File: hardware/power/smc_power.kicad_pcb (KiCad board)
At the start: 2 copper layers, 0 parts

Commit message: hw(power): label SW/BOOT/FB nets, add SW_NODE/BOOT_NODE classes, ERC clean, closes #34
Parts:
- added C1: 100nF, 25V, Capacitor_SMD:C_0805_2012Metric_Pad1.18x1.45mm_HandSolder, F.Cu at (43.1, 57.6)
- added C10: 24pF, 25V, Capacitor_SMD:C_0805_2012Metric_Pad1.18x1.45mm_HandSolder, F.Cu at (43.1, 66.6)
- added C11: 5.1nF, 25V, Capacitor_SMD:C_0805_2012Metric_Pad1.18x1.45mm_HandSolder, F.Cu at (43.1, 69.6)
- added C12: 100nF, 25V, Capacitor_SMD:C_0805_2012Metric_Pad1.18x1.45mm_HandSolder, F.Cu at (43.1, 72.7)
- added C13: 2.2uF, 100V, Capacitor_SMD:C_1206_3216Metric_Pad1.33x1.80mm_HandSolder, F.Cu at (53.3, 86.2)
- added C14: 2.2uF, 100V, Capacitor_SMD:C_1206_3216Metric_Pad1.33x1.80mm_HandSolder, F.Cu at (53.3, 89.5)
- added C15: 2.2uF, 100V, Capacitor_SMD:C_1206_3216Metric_Pad1.33x1.80mm_HandSolder, F.Cu at (53.3, 92.9)
- added C16: 47uF, 25V, Capacitor_THT:CP_Radial_D5.0mm_P2.50mm, F.Cu at (76.0, 79.5)
- added C17: 43pF, 25V, Capacitor_SMD:C_0805_2012Metric_Pad1.18x1.45mm_HandSolder, F.Cu at (47.9, 57.6)
- added C18: 2.2nF, 25V, Capacitor_SMD:C_0805_2012Metric_Pad1.18x1.45mm_HandSolder, F.Cu at (47.9, 60.6)
- added C19: 100nF 100V, Capacitor_SMD:C_0805_2012Metric_Pad1.18x1.45mm_HandSolder, F.Cu at (47.9, 63.6)
- added C2: 2.2uF, 100V, Capacitor_SMD:C_1206_3216Metric_Pad1.33x1.80mm_HandSolder, F.Cu at (53.3, 69.4)
- added C20: 470uF 100V, Capacitor_THT:CP_Radial_D16.0mm_P7.50mm, F.Cu at (28.2, 44.5)
- added C21: 470uF 100V, Capacitor_THT:CP_Radial_D16.0mm_P7.50mm, F.Cu at (28.2, 62.0)
- added C22: 0.33uF, Package_TO_SOT_SMD:SOT-89-3, F.Cu at (44.1, 77.3)
- added C23: 0.1uF, Package_TO_SOT_SMD:SOT-89-3, F.Cu at (44.1, 83.4)
- added C24: 4.7uF, Package_TO_SOT_SMD:SOT-89-3, F.Cu at (44.1, 89.5)
- added C25: 100nF 25V, Capacitor_SMD:C_0805_2012Metric_Pad1.18x1.45mm_HandSolder, F.Cu at (47.9, 66.6)
- added C26: 1uF 25V, Capacitor_SMD:C_0805_2012Metric_Pad1.18x1.45mm_HandSolder, F.Cu at (47.9, 69.6)
- added C3: 2.2uF, 100V, Capacitor_SMD:C_1206_3216Metric_Pad1.33x1.80mm_HandSolder, F.Cu at (53.3, 72.8)
- added C4: 2.2uF, 100V, Capacitor_SMD:C_1206_3216Metric_Pad1.33x1.80mm_HandSolder, F.Cu at (53.3, 76.1)
- added C5: 1uF, Capacitor_SMD:C_0805_2012Metric_Pad1.18x1.45mm_HandSolder, F.Cu at (43.1, 60.6)
- added C6: 1uF, Capacitor_SMD:C_0805_2012Metric_Pad1.18x1.45mm_HandSolder, F.Cu at (43.1, 63.6)
- added C7: 68uF, 50V, Capacitor_THT:CP_Radial_D8.0mm_P3.50mm, F.Cu at (70.6, 40.5)
- added C8: 10uF, 50V, Capacitor_SMD:C_1206_3216Metric_Pad1.33x1.80mm_HandSolder, F.Cu at (53.3, 79.5)
- added C9: 10uF, 50V, Capacitor_SMD:C_1206_3216Metric_Pad1.33x1.80mm_HandSolder, F.Cu at (53.3, 82.8)
- added D1: 100V 3A <= 850mV, Diode_SMD:D_SMB-SMC_Universal_Handsoldering, F.Cu at (61.2, 39.6)
- added D2: 100V 5A, Package_TO_SOT_SMD:TO-252-2, F.Cu at (71.8, 60.3)
- added D3: MBR10100, Step Motor Controller:TO508P482X997X1956-2P, F.Cu at (73.5, 53.4)
- added D4: SMBJ58A, Diode_SMD:D_SMA-SMB_Universal_Handsoldering, F.Cu at (60.6, 46.2)
- added D5: SS510, PCM_JLCPCB:D_SMA, F.Cu at (78.2, 70.0)
- added F1: 100V 10A, Fuse:Fuseholder_Blade_Mini_Keystone_3568, F.Cu at (60.2, 78.7)
- added IC1: LM393DR2GH, Step Motor Controller:SOIC127P600X175-8N, F.Cu at (26.9, 94.7)
- added J1: Screw_Terminal_Input, TerminalBlock_Phoenix:TerminalBlock_Phoenix_MPT-0,5-2-2.54_1x02_P2.54mm_Horizontal, F.Cu at (77.1, 88.7)
- added J2: Screw_Terminal_Output, TerminalBlock_Phoenix:TerminalBlock_Phoenix_MPT-0,5-6-2.54_1x06_P2.54mm_Horizontal, F.Cu at (58.9, 71.9)
- added L1: 68uH, Inductor_SMD:L_SXN_SMDRI125, F.Cu at (47.9, 42.6)
- added L2: 22uH, Inductor_SMD:L_Chilisin_BMRF00101040, F.Cu at (57.6, 61.9)
- added Q1: P40B10SL, Step Motor Controller:AOD4185, F.Cu at (61.2, 91.9)
- added R1: 523kR, Resistor_SMD:R_0805_2012Metric_Pad1.20x1.40mm_HandSolder, F.Cu at (25.1, 72.3)
- added R10: 15.4kR, Resistor_SMD:R_0805_2012Metric_Pad1.20x1.40mm_HandSolder, F.Cu at (29.8, 78.2)
- added R11: 18.7kR, Resistor_SMD:R_0805_2012Metric_Pad1.20x1.40mm_HandSolder, F.Cu at (29.8, 81.1)
- added R12: 11.5kR, Resistor_SMD:R_0805_2012Metric_Pad1.20x1.40mm_HandSolder, F.Cu at (29.8, 84.1)
- added R13: 97.6kR, Resistor_SMD:R_0805_2012Metric_Pad1.20x1.40mm_HandSolder, F.Cu at (29.8, 87.0)
- added R14: 243kR, Resistor_SMD:R_0805_2012Metric_Pad1.20x1.40mm_HandSolder, F.Cu at (29.8, 90.0)
- added R15: 10kR, Resistor_SMD:R_0805_2012Metric_Pad1.20x1.40mm_HandSolder, F.Cu at (34.6, 72.3)
- added R16: RX24, 50W, 33Ω, Resistor_THT:R_Axial_DIN0516_L15.5mm_D5.0mm_P25.40mm_Horizontal, F.Cu at (42.7, 52.8)
- added R17: 4.75kR, Resistor_SMD:R_0805_2012Metric_Pad1.20x1.40mm_HandSolder, F.Cu at (34.6, 75.2)
- added R18: 10R, Resistor_SMD:R_0805_2012Metric_Pad1.20x1.40mm_HandSolder, F.Cu at (34.6, 78.2)
- added R19: 1kR, Resistor_SMD:R_0805_2012Metric_Pad1.20x1.40mm_HandSolder, F.Cu at (34.6, 81.1)
- added R2: 348kR, Resistor_SMD:R_0805_2012Metric_Pad1.20x1.40mm_HandSolder, F.Cu at (25.1, 75.2)
- added R20: 10k, Resistor_SMD:R_0805_2012Metric_Pad1.20x1.40mm_HandSolder, F.Cu at (34.6, 84.1)
- added R3: 267kR, Resistor_SMD:R_0805_2012Metric_Pad1.20x1.40mm_HandSolder, F.Cu at (25.1, 78.2)
- added R4: 36.5kR, Resistor_SMD:R_0805_2012Metric_Pad1.20x1.40mm_HandSolder, F.Cu at (25.1, 81.1)
- added R5: 18.7kR, Resistor_SMD:R_0805_2012Metric_Pad1.20x1.40mm_HandSolder, F.Cu at (25.1, 84.1)
- added R6: 12kR, Resistor_SMD:R_0805_2012Metric_Pad1.20x1.40mm_HandSolder, F.Cu at (25.1, 87.0)
- added R7: 523kR, Resistor_SMD:R_0805_2012Metric_Pad1.20x1.40mm_HandSolder, F.Cu at (25.1, 90.0)
- added R8: 60.4kR, Resistor_SMD:R_0805_2012Metric_Pad1.20x1.40mm_HandSolder, F.Cu at (29.8, 72.3)
- added R9: 267kR, Resistor_SMD:R_0805_2012Metric_Pad1.20x1.40mm_HandSolder, F.Cu at (29.8, 75.2)
- added U1: TPS54360DDA, Package_SO:TI_SO-PowerPAD-8_ThermalVias, F.Cu at (70.3, 87.9)
- added U2: AP2112K-3.3, Package_TO_SOT_SMD:SOT-23-5, F.Cu at (79.6, 58.5)
- added U3: TPS54360DDA, Package_SO:TI_SO-PowerPAD-8_ThermalVias, F.Cu at (70.3, 94.6)
- added U4: TL431D, Package_SO:SOIC-8_3.9x4.9mm_P1.27mm, F.Cu at (35.4, 94.8)
- added U5: MCP1416, Package_TO_SOT_SMD:SOT-23-5, F.Cu at (79.6, 63.1)
- added U7: L78L12_SOT89, Package_TO_SOT_SMD:SOT-89-3, F.Cu at (44.1, 95.6)

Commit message: hw(power): move +VM and SS510 into project library, SS510 footprint -> Diode_SMD:D_SMA (no machine-local libs)
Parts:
- D5: footprint PCM_JLCPCB:D_SMA -> Diode_SMD:D_SMA
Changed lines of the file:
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@@
 		)
 	)
-	(footprint "PCM_JLCPCB:D_SMA"
+	(footprint "Diode_SMD:D_SMA"
 		(layer "F.Cu")
 		(at 78.185 70.025)

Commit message: hw(power): 5V output 2x22uF X7R + recompensation, inrush NTC, C22-24 footprints, refs #35, closes #38
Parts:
- added U6: TL431B_C54830630, Package_TO_SOT_SMD:SOT-23-3, F.Cu at (65.2, 119.7)
- C16: value 47uF, 25V -> 22µF 25V X7R 1210
- D4: value SMBJ58A -> SMBJ51A
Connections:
- R19 pad 1: Net-(U4-A) -> Net-(U6-K)

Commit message: hw(power): TPS16630 eFuse on 24V brake output (PGOOD LED, FLT# on J5.5), J5 -> B5B-XH-A, JLC parts to project lib, closes #55
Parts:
- added C27: 22µF 25V X7R 1210, Capacitor_SMD:C_1210_3225Metric_Pad1.33x2.70mm_HandSolder, F.Cu at (183.7, 157.4)
- added C28: 100nF, Capacitor_SMD:C_0805_2012Metric_Pad1.18x1.45mm_HandSolder, F.Cu at (187.9, 128.0)
- added D10: +5V, LED_SMD:LED_0805_2012Metric_Pad1.15x1.40mm_HandSolder, F.Cu at (183.1, 140.2)
- added D11: +3V3, LED_SMD:LED_0805_2012Metric_Pad1.15x1.40mm_HandSolder, F.Cu at (183.1, 143.2)
- added D6: +48V, LED_SMD:LED_0805_2012Metric_Pad1.15x1.40mm_HandSolder, F.Cu at (183.1, 128.0)
- added D7: +VM, LED_SMD:LED_0805_2012Metric_Pad1.15x1.40mm_HandSolder, F.Cu at (183.1, 131.1)
- added D8: +24V, LED_SMD:LED_0805_2012Metric_Pad1.15x1.40mm_HandSolder, F.Cu at (183.1, 134.1)
- added D9: +12V, LED_SMD:LED_0805_2012Metric_Pad1.15x1.40mm_HandSolder, F.Cu at (183.1, 137.1)
- added J3: 48V Output, Connector_AMASS:AMASS_XT30PW-F_1x02_P2.50mm_Horizontal, F.Cu at (165.8, 141.6)
- added J4: 24V Brake Output, Connector_JST:JST_VH_B2P-VH_1x02_P3.96mm_Vertical, F.Cu at (184.1, 149.5)
- added J5: Logic Output, Connector_JST:JST_XH_B4B-XH-A_1x04_P2.50mm_Vertical, F.Cu at (164.1, 155.3)
- added R21: NTC_5_20, Step Motor Controller:NTC_Disc_D13mm_W5.5mm_P7.5mm, F.Cu at (164.4, 148.1)
- added R22: 100kΩ, Resistor_SMD:R_0805_2012Metric_Pad1.20x1.40mm_HandSolder, F.Cu at (178.3, 128.0)
- added R23: 3.9kΩ, Resistor_SMD:R_0805_2012Metric_Pad1.20x1.40mm_HandSolder, F.Cu at (178.3, 130.9)
- added R24: 33kΩ, Resistor_SMD:R_0805_2012Metric_Pad1.20x1.40mm_HandSolder, F.Cu at (178.3, 133.9)
- added R25: 33kΩ, Resistor_SMD:R_0805_2012Metric_Pad1.20x1.40mm_HandSolder, F.Cu at (178.3, 136.8)
- added R26: 15kΩ, Resistor_SMD:R_0805_2012Metric_Pad1.20x1.40mm_HandSolder, F.Cu at (178.3, 139.8)
- added R27: 6.8kΩ, Resistor_SMD:R_0805_2012Metric_Pad1.20x1.40mm_HandSolder, F.Cu at (178.3, 142.7)
- added R28: 2kΩ, Resistor_SMD:R_0805_2012Metric_Pad1.20x1.40mm_HandSolder, F.Cu at (178.3, 145.7)
- added R29: 820Ω, Resistor_SMD:R_0805_2012Metric_Pad1.20x1.40mm_HandSolder, F.Cu at (178.3, 148.6)
- C16: footprint Capacitor_THT:CP_Radial_D5.0mm_P2.50mm -> Capacitor_SMD:C_1210_3225Metric_Pad1.33x2.70mm_HandSolder
- C17: value 43pF, 25V -> 220pF, 25V
- C18: value 2.2nF, 25V -> 27nF, 25V
- C22, C23, C24: footprint Package_TO_SOT_SMD:SOT-89-3 -> Capacitor_SMD:C_0805_2012Metric_Pad1.18x1.45mm_HandSolder
- J1: value Screw_Terminal_Input -> Screw_Terminal_01x02; footprint TerminalBlock_Phoenix:TerminalBlock_Phoenix_MPT-0,5-2-2.54_1x02_P2.54mm_Horizontal -> TerminalBlock_Phoenix:TerminalBlock_Phoenix_MKDS-1,5-2-5.08_1x02_P5.08mm_Horizontal
- J2: value Screw_Terminal_Output -> 48V Input; footprint TerminalBlock_Phoenix:TerminalBlock_Phoenix_MPT-0,5-6-2.54_1x06_P2.54mm_Horizontal -> Connector_AMASS:AMASS_XT60PW-M_1x02_P7.20mm_Horizontal
- R10: value 15.4kR -> 4.22kR
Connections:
- D3 pad 1: +VM -> Net-(D3-K)
- D5 pad 2: Net-(Q1-D) -> Net-(J1-Pin_2)
- F1 pad 1: +48V -> Net-(D3-A)
- F1 pad 2: Net-(D3-A) -> +48V
- J1 pad 1: GND -> +VM
- J1 pad 2: +48V -> Net-(J1-Pin_2)
- J2 pad 1: GND -> +48V
- J2 pad 2: +3V3 -> GND
- Q1 pad 2: Net-(Q1-D) -> Net-(J1-Pin_2)
- R19 pad 1: Net-(U6-K) -> Net-(IC1-INPUT_A_1)
- U6 pad 2: Net-(U6-K) -> Net-(IC1-INPUT_A_1)

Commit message: hw(power): 48V input DM pi-filter (L4 2.2uH ETQP4M2R2KVK, C34/C35 2.2uF 100V X7R), closes #65
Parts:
- moved J2 64.0 mm to (118.0, 47.3)
- moved R21 16.8 mm to (147.6, 147.7)
- moved D3 4.81 mm to (77.8, 51.3)
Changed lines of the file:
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@@
 	(footprint "Step Motor Controller:TO508P482X997X1956-2P"
 		(layer "F.Cu")
-		(at 73.45 53.435)
+		(at 77.76 51.3)
 		(descr "TO−220, 2−LEAD CASE 221B−04 ISSUE F_2025")
 		(tags "Schottky Diode")
@@
 	(footprint "Connector_AMASS:AMASS_XT60PW-M_1x02_P7.20mm_Horizontal"
 		(layer "F.Cu")
-		(at 58.875 71.875)
+		(at 117.95 47.3)
 		(descr "Connector XT60 Horizontal PCB Female, https://www.tme.eu/Document/b13629717d44ae038681dba08d18c0b6/XT60PW-M.pdf")
 		(tags "RC Connector XT60")
@@
 	(footprint "Step Motor Controller:NTC_Disc_D13mm_W5.5mm_P7.5mm"
 		(layer "F.Cu")
-		(at 164.375 148.125)
+		(at 147.55 147.7)
 		(descr "Power NTC thermistor, radial disc D13mm (max) x 5.5mm, lead pitch 7.5mm, lead 0.8mm (MF72 5D11)")
 		(tags "NTC thermistor disc radial MF72")

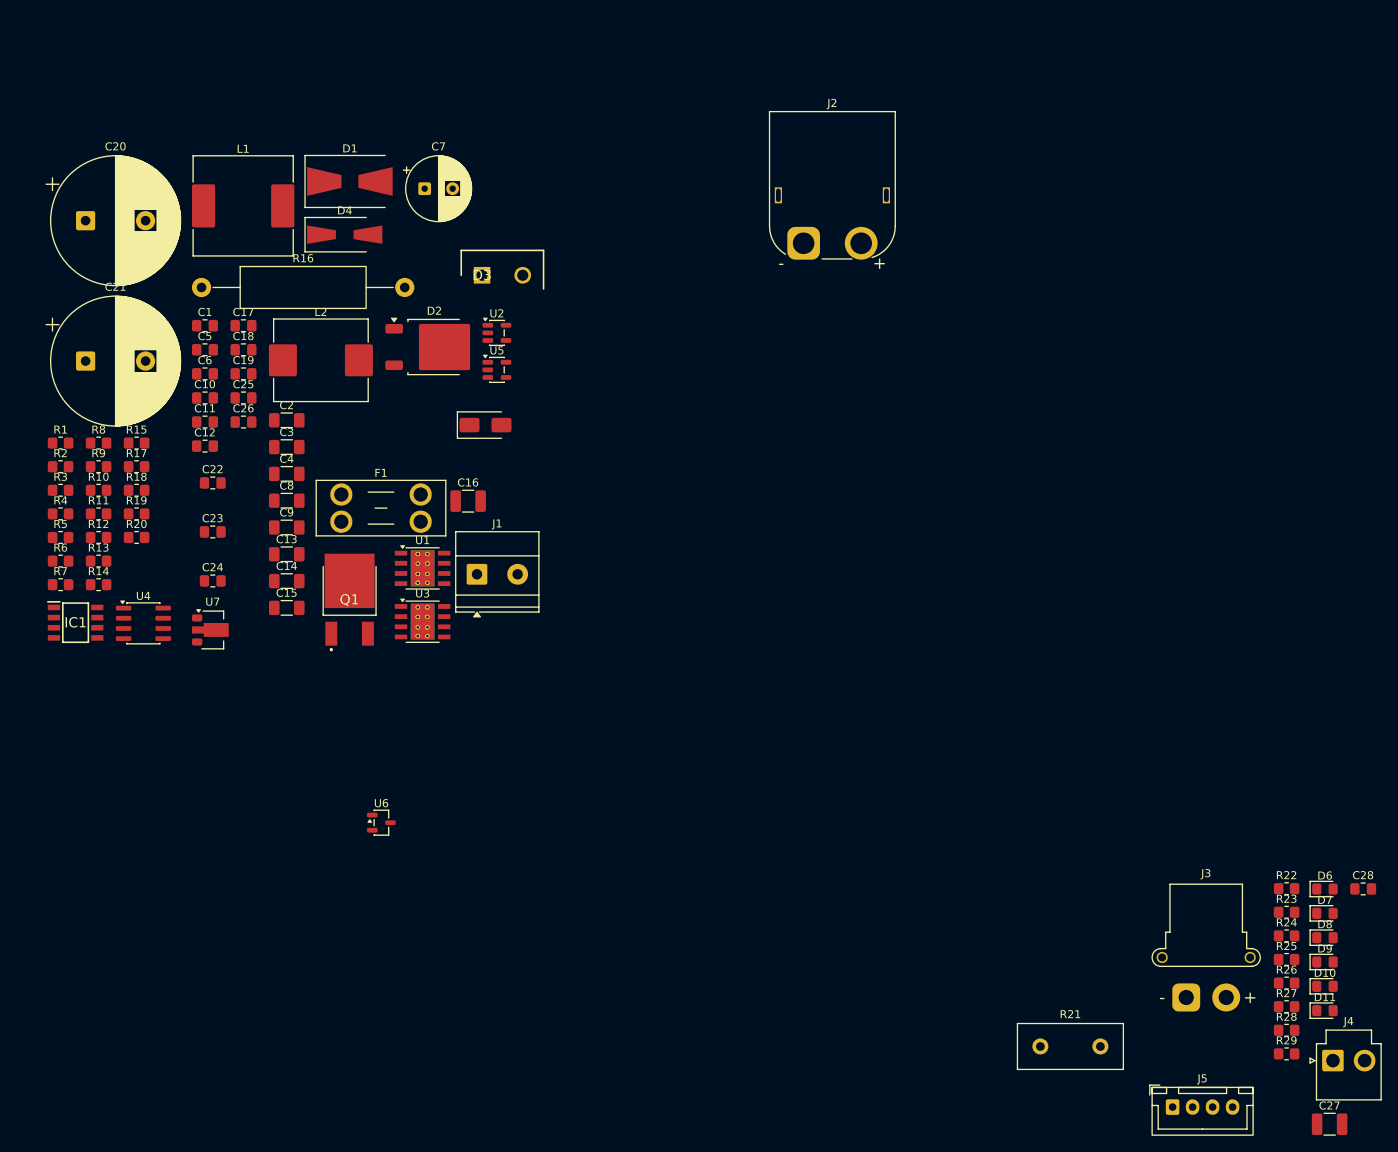
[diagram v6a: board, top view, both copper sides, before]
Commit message: hw(power): 4-layer 2oz/1oz stackup, PCB synced from schematic, refs #39
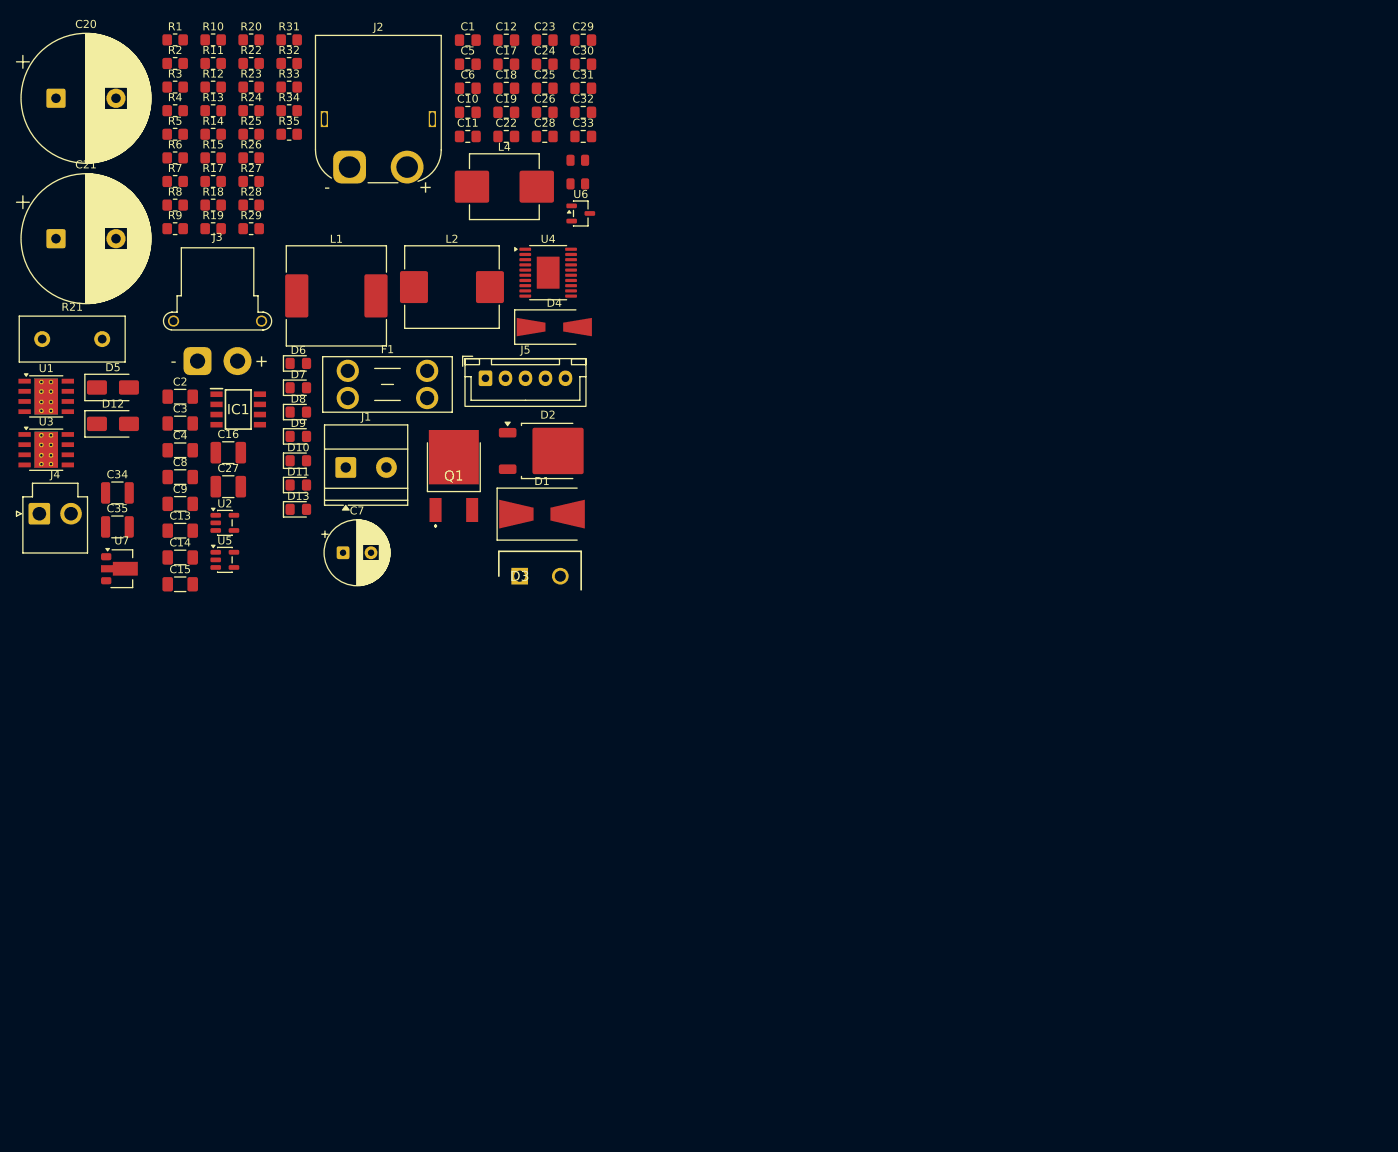
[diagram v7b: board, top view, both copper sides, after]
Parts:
- removed R16: RX24, 50W, 33Ω, Resistor_THT:R_Axial_DIN0516_L15.5mm_D5.0mm_P25.40mm_Horizontal
- added C29: 22nF, Capacitor_SMD:C_0805_2012Metric_Pad1.18x1.45mm_HandSolder, F.Cu at (90.4, 21.9)
- added C30: 1uF, Capacitor_SMD:C_0805_2012Metric_Pad1.18x1.45mm_HandSolder, F.Cu at (90.4, 24.9)
- added C31: 100nF, Capacitor_SMD:C_0805_2012Metric_Pad1.18x1.45mm_HandSolder, F.Cu at (90.4, 27.9)
- added C32: 10uF, Capacitor_SMD:C_0805_2012Metric_Pad1.18x1.45mm_HandSolder, F.Cu at (90.4, 30.9)
- added C33: 100nF, Capacitor_SMD:C_0805_2012Metric_Pad1.18x1.45mm_HandSolder, F.Cu at (90.4, 33.9)
- added C34: CL32B225KCJSNNE, Capacitor_SMD:C_1210_3225Metric, F.Cu at (32.2, 78.5)
- added C35: CL32B225KCJSNNE, Capacitor_SMD:C_1210_3225Metric, F.Cu at (32.2, 82.8)
- added D12: SS510, Diode_SMD:D_SMA, F.Cu at (31.6, 69.9)
- added D13: 24V BRK FLT, LED_SMD:LED_0805_2012Metric_Pad1.15x1.40mm_HandSolder, F.Cu at (54.8, 80.6)
- added L4: ETQP4M2R2KVK, Inductor_SMD:L_Panasonic_PCC-M0850M, F.Cu at (80.5, 40.2)
- added R30: 12kΩ, PCM_JLCPCB:R_0805, F.Cu at (89.7, 36.9)
- added R31: 953kΩ, Resistor_SMD:R_0805_2012Metric_Pad1.20x1.40mm_HandSolder, F.Cu at (53.6, 21.9)
- added R32: 20kΩ, Resistor_SMD:R_0805_2012Metric_Pad1.20x1.40mm_HandSolder, F.Cu at (53.6, 24.8)
- added R33: 40.2kΩ, Resistor_SMD:R_0805_2012Metric_Pad1.20x1.40mm_HandSolder, F.Cu at (53.6, 27.8)
- added R34: 10kΩ, Resistor_SMD:R_0805_2012Metric_Pad1.20x1.40mm_HandSolder, F.Cu at (53.6, 30.7)
- added R35: 1kΩ, Resistor_SMD:R_0805_2012Metric_Pad1.20x1.40mm_HandSolder, F.Cu at (53.6, 33.7)
- added R36: 0Ω, PCM_JLCPCB:R_0805, F.Cu at (89.7, 39.9)
- J5: footprint Connector_JST:JST_XH_B4B-XH-A_1x04_P2.50mm_Vertical -> Connector_JST:JST_XH_B5B-XH-A_1x05_P2.50mm_Vertical
- U4: value TL431D -> TPS16630PWPR; footprint Package_SO:SOIC-8_3.9x4.9mm_P1.27mm -> Package_SO:HTSSOP-20-1EP_4.4x6.5mm_P0.65mm_EP2.85x4mm
- moved J4 175.6 mm to (22.4, 81.1)
- moved R22 165.5 mm to (48.9, 24.8)
- moved R23 165.5 mm to (48.9, 27.8)
- moved R24 165.5 mm to (48.9, 30.7)
- moved R25 165.5 mm to (48.9, 33.7)
- moved R26 165.5 mm to (48.9, 36.6)
- moved R27 165.5 mm to (48.9, 39.6)
- moved R28 165.5 mm to (48.9, 42.5)
- moved R29 165.5 mm to (48.9, 45.5)
- moved C27 159.1 mm to (46.0, 77.7)
- moved R21 152.9 mm to (22.8, 59.3)
- moved J3 147.0 mm to (42.2, 62.0)
- moved D10 144.2 mm to (54.8, 74.5)
- moved D11 144.2 mm to (54.8, 77.5)
- moved D6 144.2 mm to (54.8, 62.3)
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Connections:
- net Net-(D3-A) renamed /VIN_FUSED
- net Net-(D3-K) renamed /VIN_PROT
- net Net-(J1-Pin_2) renamed /CHOP_DRAIN
- J4 pad 1: +24V -> /+24V_BRK
- R19 pad 1: Net-(IC1-INPUT_A_1) -> Net-(U6-K)
- R21 pad 1: +VM -> /VIN_EMI
- U4 pad 1: GND -> +24V
- U4 pad 2: Net-(U4-A) -> +24V
- U4 pad 3: Net-(U4-A) -> +24V
- U4 pad 4: (no net) -> unconnected-(U4-N.C-Pad4)
- U4 pad 5: (no net) -> unconnected-(U4-N.C-Pad5)
- U4 pad 6: Net-(U4-A) -> +24V
- U4 pad 7: Net-(U4-A) -> Net-(U4-UVLO)
- U4 pad 8: Net-(IC1-INPUT_A_1) -> Net-(U4-OVP)
- U6 pad 2: Net-(IC1-INPUT_A_1) -> Net-(U6-K)
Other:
- copper layers 2 -> 4

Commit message: hw(power): re-apply project-lib fixes overwritten by KiCad save (+VM, R30/R36, L4 LCSC), refs #39
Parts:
- R30, R36: footprint PCM_JLCPCB:R_0805 -> Resistor_SMD:R_0805_2012Metric_Pad1.20x1.40mm_HandSolder
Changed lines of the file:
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@@
 		)
 	)
-	(footprint "PCM_JLCPCB:R_0805"
+	(footprint "Resistor_SMD:R_0805_2012Metric_Pad1.20x1.40mm_HandSolder"
 		(layer "F.Cu")
 		(at 89.725 39.875)
@@
 		)
 	)
-	(footprint "PCM_JLCPCB:R_0805"
+	(footprint "Resistor_SMD:R_0805_2012Metric_Pad1.20x1.40mm_HandSolder"
 		(layer "F.Cu")
 		(at 89.725 36.925)
